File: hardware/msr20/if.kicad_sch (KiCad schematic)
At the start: 16 parts, among them U14 AD7478, U15 MC1350, U16 LTC455-FU

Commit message: assign footprints to passives in if stage
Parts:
- C25, C26, C27, C28, C31: footprint (none) -> Capacitor_SMD:C_0805_2012Metric
- L10, L7, L8, L9: footprint (none) -> Inductor_SMD:L_0805_2012Metric
- R8, R9: footprint (none) -> Resistor_SMD:R_0805_2012Metric
- U15: footprint (none) -> Package_DIP:DIP-8_W7.62mm_LongPads
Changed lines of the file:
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@@
 			)
 		)
-		(property "Footprint" ""
+		(property "Footprint" "Capacitor_SMD:C_0805_2012Metric"
 			(at 127.9652 73.66 0)
 			(effects
@@
 			)
 		)
-		(property "Footprint" ""
+		(property "Footprint" "Inductor_SMD:L_0805_2012Metric"
 			(at 96.52 88.9 0)
 			(effects
@@
 			)
 		)
-		(property "Footprint" ""
+		(property "Footprint" "Capacitor_SMD:C_0805_2012Metric"
 			(at 118.11 87.9348 0)
 			(effects
@@
 			)
 		)
-		(property "Footprint" ""
+		(property "Footprint" "Inductor_SMD:L_0805_2012Metric"
 			(at 168.91 69.85 0)
 			(effects
@@
 			)
 		)
-		(property "Footprint" ""
+		(property "Footprint" "Capacitor_SMD:C_0805_2012Metric"
 			(at 126.0348 78.74 0)
 			(effects
@@
 			)
 		)
-		(property "Footprint" ""
+		(property "Footprint" "Capacitor_SMD:C_0805_2012Metric"
 			(at 143.51 62.5348 0)
 			(effects
@@
 			)
 		)
-		(property "Footprint" ""
+		(property "Footprint" "Inductor_SMD:L_0805_2012Metric"
 			(at 168.91 57.15 0)
 			(effects
@@
 			)
 		)
-		(property "Footprint" ""
+		(property "Footprint" "Resistor_SMD:R_0805_2012Metric"
 			(at 167.132 82.55 90)
 			(effects
@@
 			)
 		)
-		(property "Footprint" ""
+		(property "Footprint" "Resistor_SMD:R_0805_2012Metric"
 			(at 131.572 107.95 90)
 			(effects
@@
 			)
 		)
-		(property "Footprint" ""
+		(property "Footprint" "Package_DIP:DIP-8_W7.62mm_LongPads"
 			(at 152.4 76.2 0)
 			(effects
@@
 			)
 		)
-		(property "Footprint" ""
+		(property "Footprint" "Capacitor_SMD:C_0805_2012Metric"
 			(at 144.4752 111.76 0)
 			(effects
@@
 			)
 		)
-		(property "Footprint" ""
+		(property "Footprint" "Inductor_SMD:L_0805_2012Metric"
 			(at 52.07 88.9 0)
 			(effects

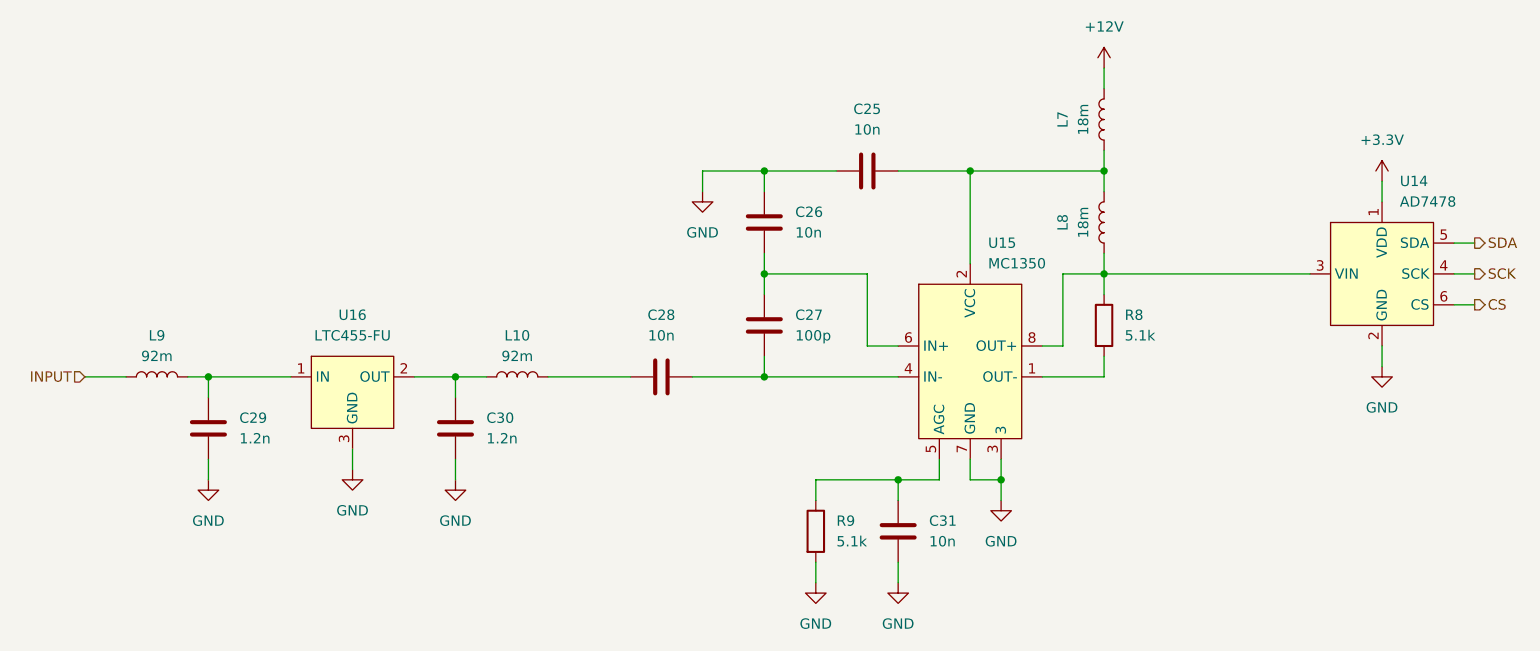
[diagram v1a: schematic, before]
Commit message: add test points to schematic
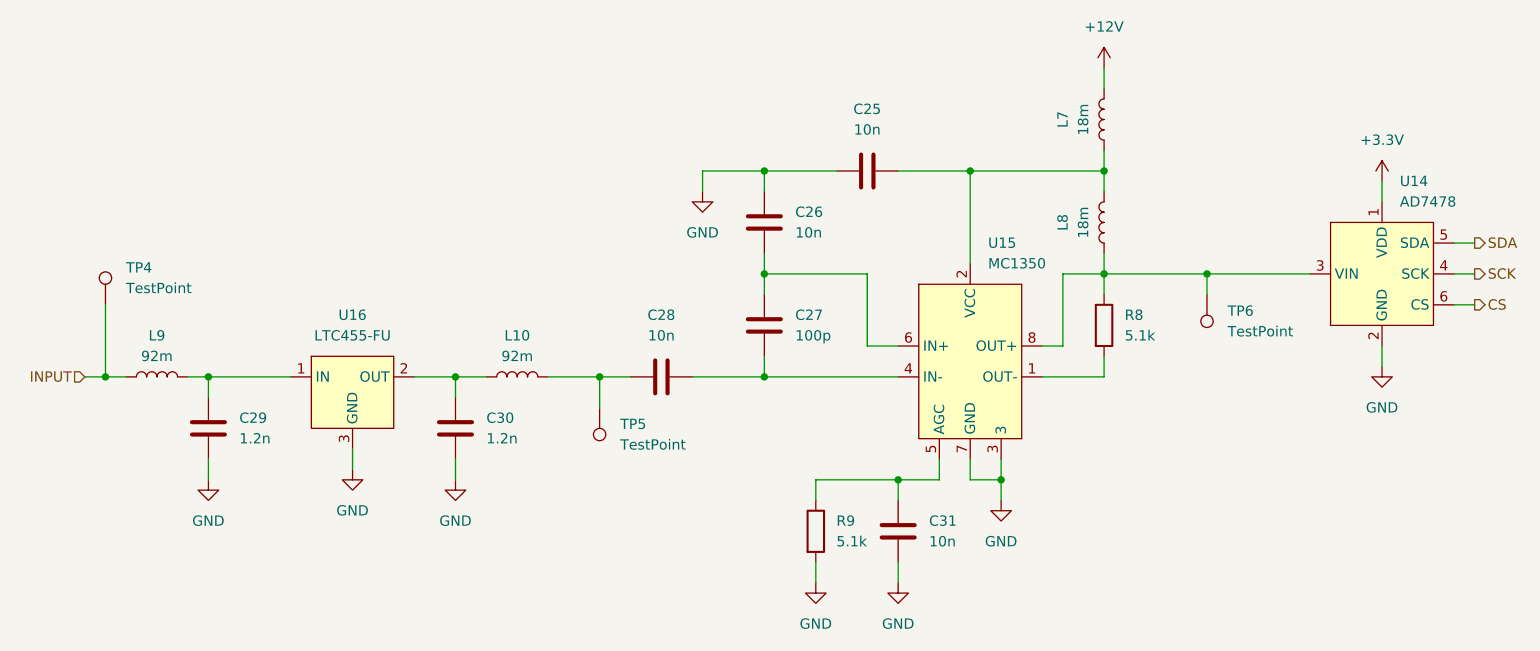
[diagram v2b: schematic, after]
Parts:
- added TP4, TP5, TP6: TestPoint, TestPoint:TestPoint_Pad_D1.0mm, symbol Connector:TestPoint
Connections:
- net INPUT: now also TP4.1
- net at C28.1, L10.2: now also TP5.1
- net at L8.1, R8.1, U14.3 (VIN)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: now also TP6.1

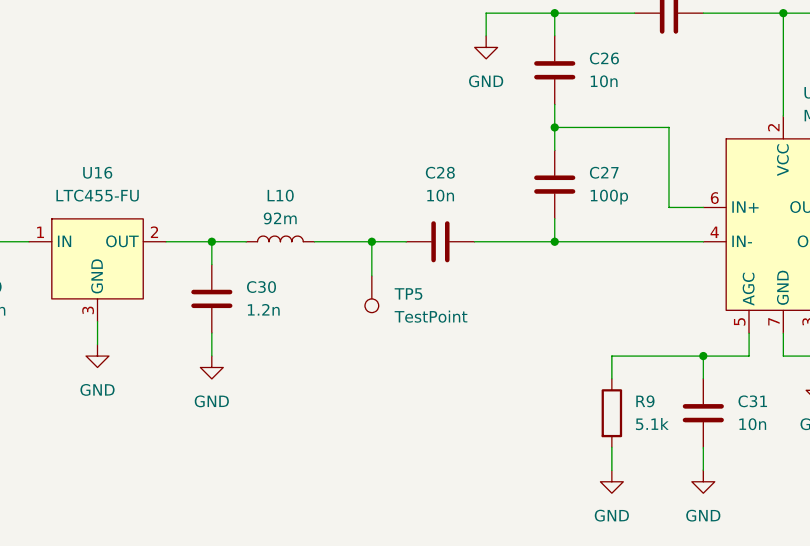
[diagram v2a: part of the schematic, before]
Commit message: power and ground routing
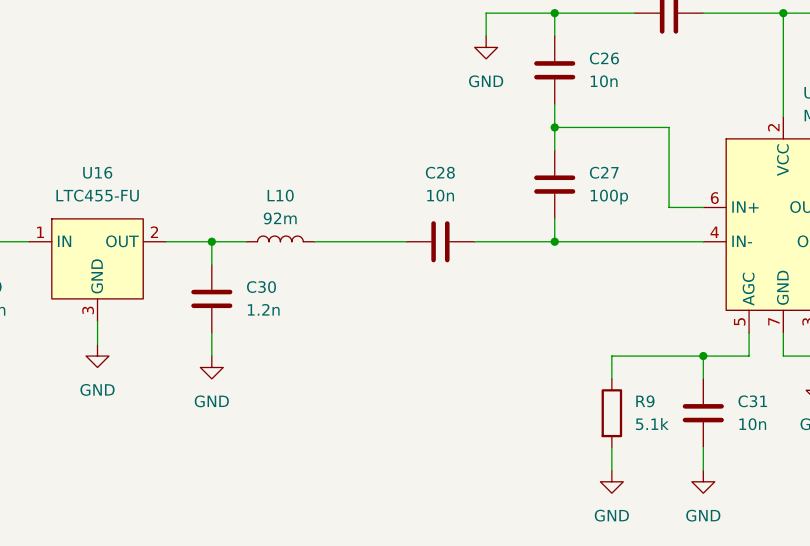
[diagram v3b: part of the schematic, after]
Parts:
- removed TP5: TestPoint, TestPoint:TestPoint_Pad_D1.0mm, symbol Connector:TestPoint
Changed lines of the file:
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@@
-	)
-	(junction
-		(at 106.68 88.9)
-		(diameter 0)
-		(color 0 0 0 0)
 	)
 	(junction
@@
 	(wire
 		(pts
-			(xy 106.68 88.9) (xy 110.49 88.9)
+			(xy 100.33 88.9) (xy 110.49 88.9)
 		)
 		(stroke
@@
 	(wire
 		(pts
-			(xy 106.68 88.9) (xy 106.68 92.71)
-		)
-		(stroke
-			(width 0)
-			(type default)
-		)
-	)
-	(wire
-		(pts
 			(xy 152.4 99.06) (xy 152.4 101.6)
 		)
@@
 		(pts
 			(xy 163.83 76.2) (xy 168.91 76.2)
-		)
-		(stroke
-			(width 0)
-			(type default)
-		)
-	)
-	(wire
-		(pts
-			(xy 100.33 88.9) (xy 106.68 88.9)
 		)
 		(stroke
@@
 					(unit 1)
 				)
-			)
-		)
-	)
-	(symbol
-		(lib_id "Connector:TestPoint")
-		(at 106.68 92.71 180)
-		(unit 1)
-		(exclude_from_sim no)
-		(in_bom yes)
-		(on_board yes)
-		(dnp no)
-		(fields_autoplaced yes)
-		(property "Reference" "TP5"
-			(at 109.22 94.7419 0)
-			(effects
-				(font
-					(size 1.27 1.27)
-				)
-				(justify right)
-			)
-		)
-		(property "Value" "TestPoint"
-			(at 109.22 97.2819 0)
-			(effects
-				(font
-					(size 1.27 1.27)
-				)
-				(justify right)
-			)
-		)
-		(property "Footprint" "TestPoint:TestPoint_Pad_D1.0mm"
-			(at 101.6 92.71 0)
-			(effects
-				(font
-					(size 1.27 1.27)
-				)
-				(hide yes)
-			)
-		)
-		(property "Datasheet" "~"
-			(at 101.6 92.71 0)
-			(effects
-				(font
-					(size 1.27 1.27)
-				)
-				(hide yes)
-			)
-		)
-		(property "Description" "test point"
-			(at 106.68 92.71 0)
-			(effects
-				(font
-					(size 1.27 1.27)
-				)
-				(hide yes)
-			)
-		)
-		(pin "1"
-		)
-		(instances
-			(project "msr20"
-				(path "/827e4c90-6b76-4aba-b6da-8b66ea005818/585458a5-998e-4f63-a5a4-45d71155a4e5"
-					(reference "TP5")
-					(unit 1)
-				)
